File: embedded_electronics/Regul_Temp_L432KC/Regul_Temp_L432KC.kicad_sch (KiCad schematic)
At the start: 28 parts, among them J1 TRIM_CONSIGNE, J10 MOT_OUT, J11 Digilent Motor, J12 2.54 motor, J2 Temp_In, J3 POWER_IN_5V, J4 SW_MODE, J5 OUT_to_BNC, J6 Consigne, J7 Erreur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

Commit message: Update Regul temp
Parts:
- added J13: Consigne_In, Connector_PinSocket_2.54mm:PinSocket_1x02_P2.54mm_Vertical, symbol Connector_Generic:Conn_01x02
- added J14: SW_consigne, Connector_PinSocket_2.54mm:PinSocket_1x03_P2.54mm_Vertical, symbol Connector_Generic:Conn_01x03
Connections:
- net GND: now also J13.1 (Pin_1)
- net at U1.5 (+): now also J14.2 (Pin_2); no longer J1.2 (Pin_2)
- new net In_consigne: J13.2 (Pin_2), J14.1 (Pin_1)
- new net T_consigne: J1.2 (Pin_2), J14.3 (Pin_3)
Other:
- moved on the sheet: J1, U1B

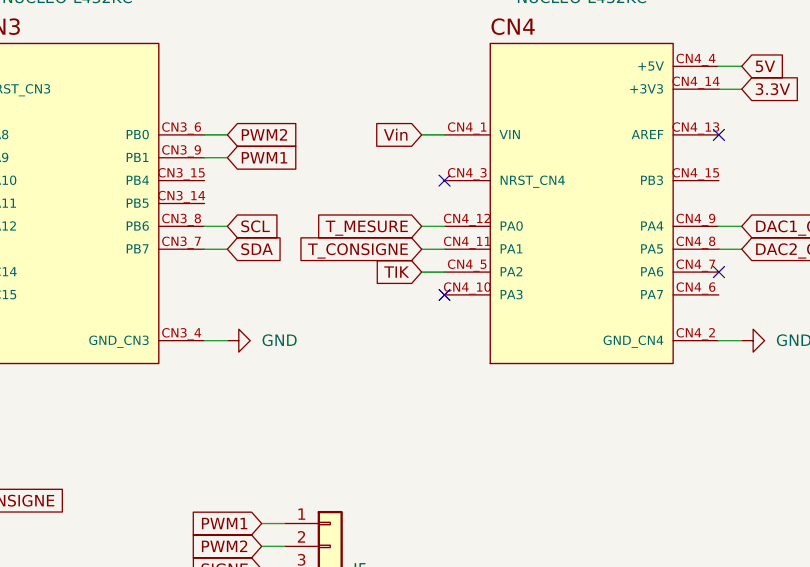
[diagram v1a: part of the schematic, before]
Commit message: Update Regul Temp / Debugging LCD screen and test of Follower
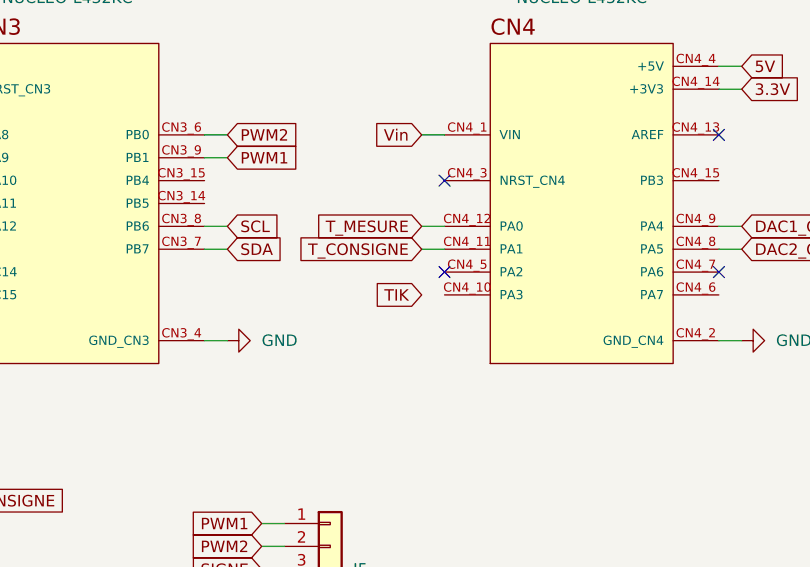
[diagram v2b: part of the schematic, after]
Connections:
- net TIK: no longer U2.CN4_5 (PA2)
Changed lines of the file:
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@@
+	)
+	(no_connect
+		(at 146.05 63.5)
 	)
 	(no_connect
@@
 	)
 	(no_connect
-		(at 146.05 66.04)
-	)
-	(no_connect
 		(at 88.9 43.18)
 	)
@@
 		(pts
 			(xy 35.56 119.38) (xy 35.56 121.92)
-		)
-		(stroke
-			(width 0)
-			(type default)
-		)
-	)
-	(wire
-		(pts
-			(xy 143.51 63.5) (xy 146.05 63.5)
 		)
 		(stroke
@@
 	(global_label "TIK"
 		(shape input)
-		(at 143.51 63.5 180)
+		(at 143.51 66.04 180)
 		(fields_autoplaced yes)
 		(effects
@@
 		)
 		(property "Intersheetrefs" "${INTERSHEET_REFS}"
-			(at 137.6824 63.5 0)
+			(at 137.6824 66.04 0)
 			(effects
 				(font
